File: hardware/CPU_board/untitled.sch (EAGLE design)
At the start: 60 parts, among them IC1 MAX232ECWE, IC2 MAX232ECWE, IC3 AM29F040J, IC4 74HCT138D, IC5 LM2596S, J2 POWER_JACKSLT, U1 AS6C4008-55SIN, Y1 CRYSTAL-GROUNDEDSMD-5X3.2

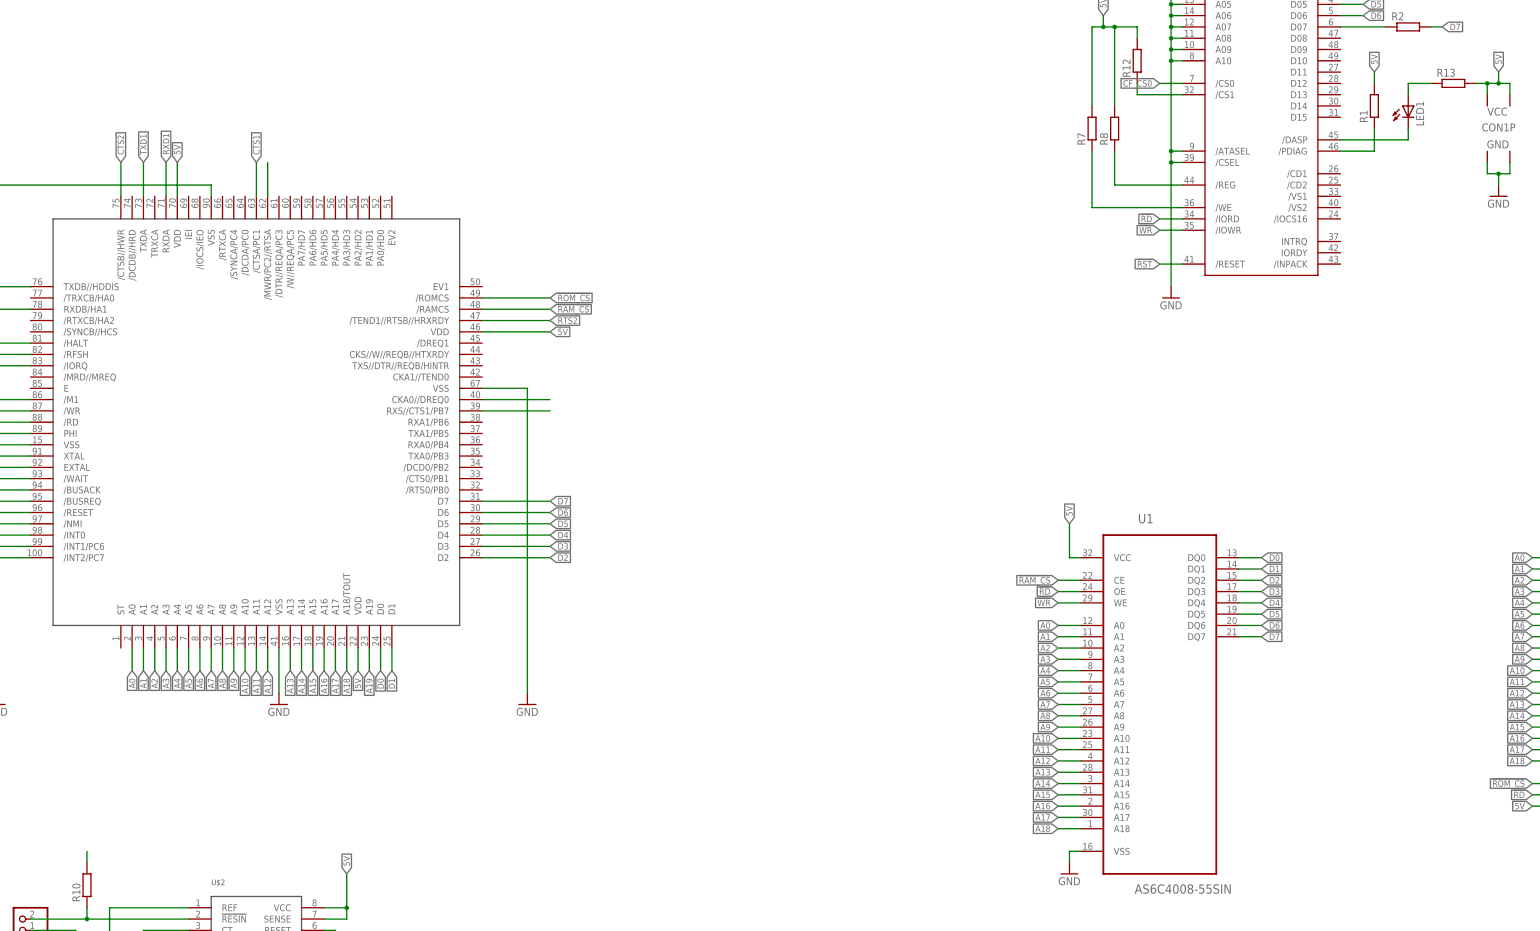
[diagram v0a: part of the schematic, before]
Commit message: Connector instead LED on board
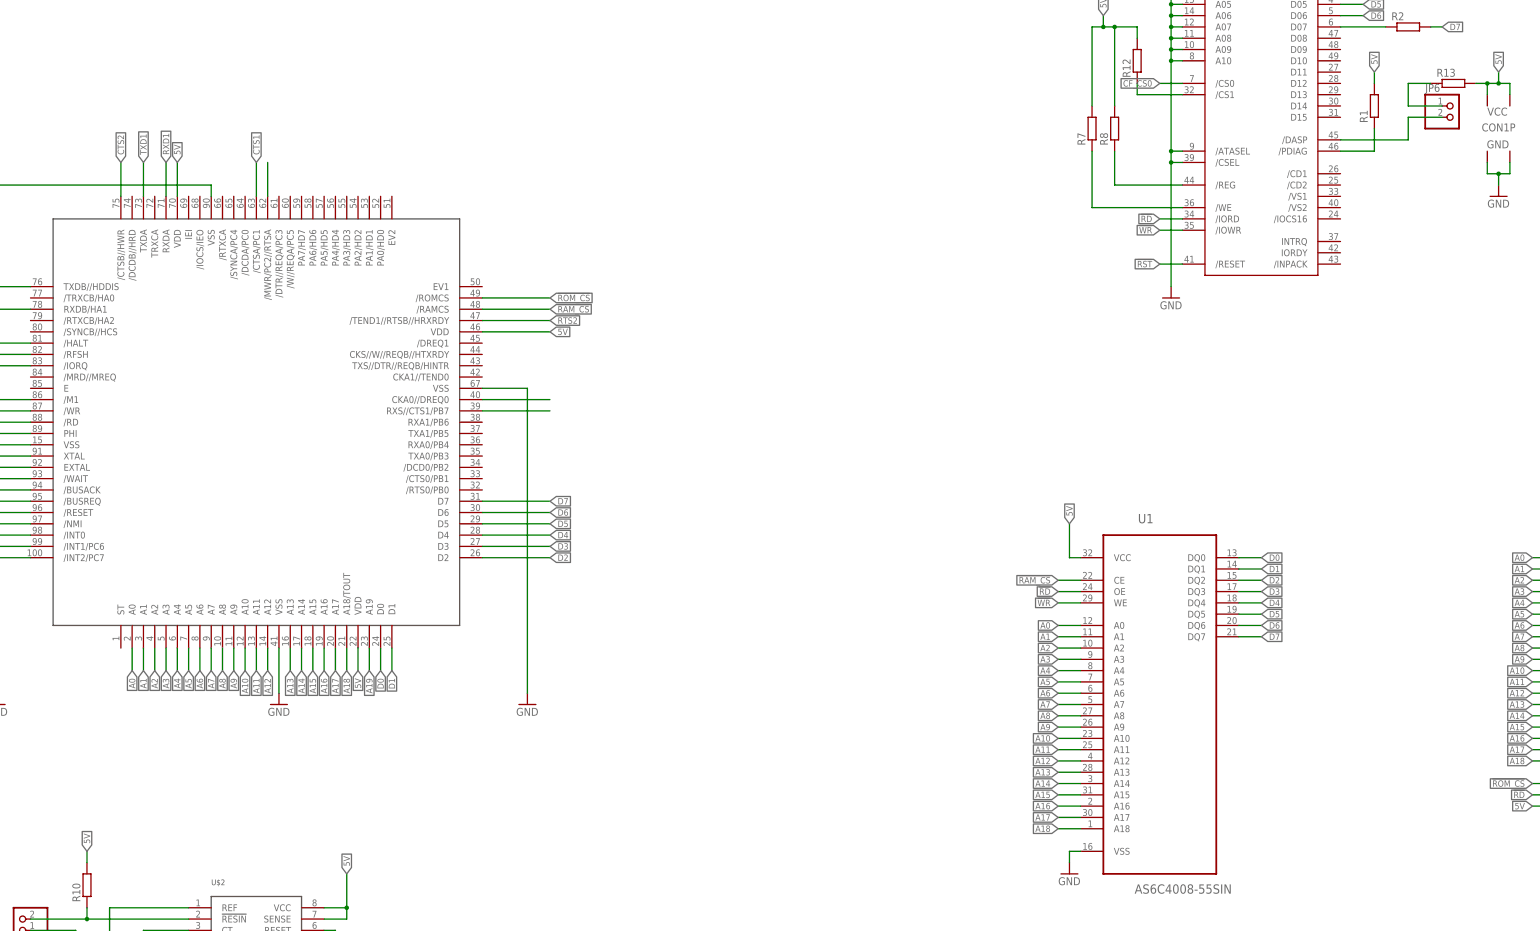
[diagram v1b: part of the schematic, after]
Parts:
- removed LED1: (no value), led:LED5MM
- added JP6: (no value), pinhead:PINHD-1X2
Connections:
- net N$32: now also JP6.1; no longer LED1.A
- net N$33: now also JP6.2; no longer LED1.C
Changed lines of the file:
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@@
 <part name="R12" library="rcl" deviceset="R-EU_" device="R0603"/>
 <part name="R13" library="rcl" deviceset="R-EU_" device="R0603"/>
-<part name="LED1" library="led" deviceset="LED" device="5MM"/>
 <part name="R2" library="rcl" deviceset="R-EU_" device="R0603"/>
 <part name="IC4" library="74xx-eu" deviceset="74*138" device="D" technology="HCT"/>
@@
 <part name="GND16" library="supply1" deviceset="GND" device=""/>
 <part name="R10" library="rcl" deviceset="R-EU_" device="R0603"/>
+<part name="JP6" library="pinhead" deviceset="PINHD-1X2" device=""/>
 </parts>
 <sheets>
@@
 <instance part="R12" gate="G$1" x="284.48" y="167.64" rot="R90"/>
 <instance part="R13" gate="G$1" x="355.6" y="162.56"/>
-<instance part="LED1" gate="G$1" x="345.44" y="157.48"/>
 <instance part="R2" gate="G$1" x="345.44" y="175.26"/>
 <instance part="IC4" gate="A" x="-203.2" y="15.24"/>
@@
 <instance part="GND16" gate="1" x="45.72" y="-45.72"/>
 <instance part="R10" gate="G$1" x="48.26" y="-17.78" rot="R90"/>
+<instance part="JP6" gate="G$1" x="355.6" y="154.94"/>
 </instances>
 <busses>
@@
 <pinref part="R10" gate="G$1" pin="2"/>
 <wire x1="48.26" y1="-12.7" x2="48.26" y2="-10.16" width="0.1524" layer="91"/>
+<label x="48.26" y="-10.16" size="1.4224" layer="95" rot="R90" xref="yes"/>
 </segment>
 </net>
@@
 <segment>
 <pinref part="R13" gate="G$1" pin="1"/>
-<pinref part="LED1" gate="G$1" pin="A"/>
 <wire x1="350.52" y1="162.56" x2="345.44" y2="162.56" width="0.1524" layer="91"/>
-<wire x1="345.44" y1="162.56" x2="345.44" y2="160.02" width="0.1524" layer="91"/>
+<pinref part="JP6" gate="G$1" pin="1"/>
+<wire x1="353.06" y1="157.48" x2="345.44" y2="157.48" width="0.1524" layer="91"/>
+<wire x1="345.44" y1="157.48" x2="345.44" y2="162.56" width="0.1524" layer="91"/>
 </segment>
 </net>
@@
 <segment>
 <pinref part="CON1" gate="G$1" pin="/DASP"/>
-<pinref part="LED1" gate="G$1" pin="C"/>
 <wire x1="330.2" y1="149.86" x2="345.44" y2="149.86" width="0.1524" layer="91"/>
-<wire x1="345.44" y1="149.86" x2="345.44" y2="152.4" width="0.1524" layer="91"/>
-</segment>
-</net>
+<pinref part="JP6" gate="G$1" pin="2"/>
+<wire x1="353.06" y1="154.94" x2="345.44" y2="154.94" width="0.1524" layer="91"/>
+<wire x1="345.44" y1="154.94" x2="345.44" y2="149.86" width="0.1524" layer="91"/>
+</segment>
+</net>

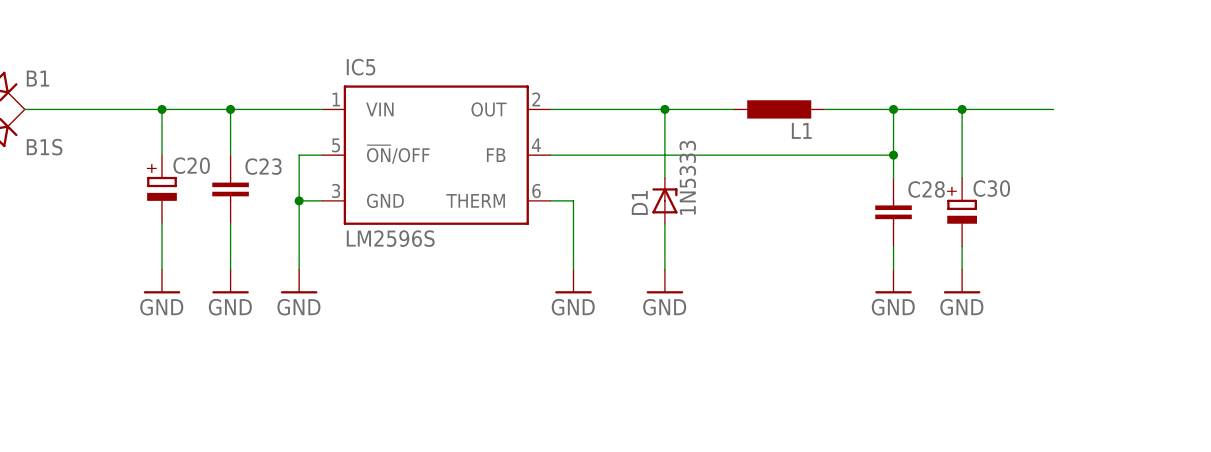
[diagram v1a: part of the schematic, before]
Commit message: Power circuit updated
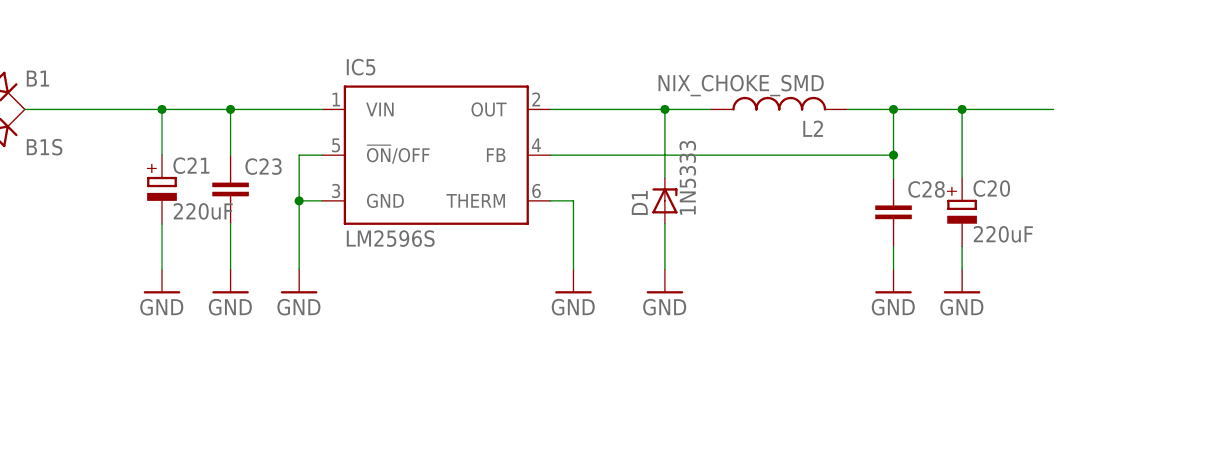
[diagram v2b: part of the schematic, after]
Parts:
- removed C30: (no value), rcl:CPOL-EUE3.5-8
- removed L1: (no value), rcl:L-EU6000-XXX-RC
- added C21: 220uF, rcl:CPOL-EU153CLV-0810
- added L2: NIX_CHOKE_SMD, mw:NIX_CHOKE_SMD
- C20: value (none) -> 220uF; device rcl:CPOL-EUE3.5-8 -> rcl:CPOL-EU153CLV-0810
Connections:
- net 5V: now also C20.+, L2.2; no longer C30.+, L1.2
- net GND: now also C21.-; no longer C30.-
- net N$22: now also C21.+; no longer C20.+
- net N$23: now also L2.1; no longer L1.1
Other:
- moved on the sheet: C20
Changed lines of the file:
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@@
 <part name="F1" library="polyfuse-smd_10" deviceset="?" device="1206L" technology="012" value="1206L012"/>
 <part name="J2" library="SparkFun-Connectors" deviceset="POWER_JACK" device="SLT"/>
-<part name="C20" library="rcl" deviceset="CPOL-EU" device="E3.5-8"/>
 <part name="GND52" library="supply1" deviceset="GND" device=""/>
 <part name="GND58" library="supply1" deviceset="GND" device=""/>
@@
 <part name="GND34" library="supply1" deviceset="GND" device=""/>
 <part name="GND56" library="supply1" deviceset="GND" device=""/>
-<part name="L1" library="rcl" deviceset="L-EU" device="6000-XXX-RC"/>
-<part name="C30" library="rcl" deviceset="CPOL-EU" device="E3.5-8"/>
 <part name="GND57" library="supply1" deviceset="GND" device=""/>
 <part name="U1" library="Alliance_Memory_By_element14_Batch_1" deviceset="AS6C4008-55SIN" device=""/>
@@
 <part name="R10" library="rcl" deviceset="R-EU_" device="R0603"/>
 <part name="JP6" library="pinhead" deviceset="PINHD-1X2" device=""/>
+<part name="C21" library="rcl" deviceset="CPOL-EU" device="153CLV-0810" value="220uF"/>
+<part name="C20" library="rcl" deviceset="CPOL-EU" device="153CLV-0810" value="220uF"/>
+<part name="L2" library="mw" deviceset="NIX_CHOKE_SMD" device=""/>
 </parts>
 <sheets>
@@
 <instance part="F1" gate="G$1" x="-236.22" y="274.32" rot="R180"/>
 <instance part="J2" gate="G$1" x="-248.92" y="266.7"/>
-<instance part="C20" gate="G$1" x="-195.58" y="266.7"/>
 <instance part="GND52" gate="1" x="-195.58" y="254"/>
 <instance part="GND58" gate="1" x="-180.34" y="254"/>
@@
 <instance part="GND34" gate="1" x="-114.3" y="254"/>
 <instance part="GND56" gate="1" x="-187.96" y="254"/>
-<instance part="L1" gate="G$1" x="-127" y="274.32" rot="R90"/>
-<instance part="C30" gate="G$1" x="-106.68" y="264.16"/>
 <instance part="GND57" gate="1" x="-106.68" y="254"/>
 <instance part="U1" gate="A" x="289.56" y="25.4"/>
@@
 <instance part="R10" gate="G$1" x="48.26" y="-17.78" rot="R90"/>
 <instance part="JP6" gate="G$1" x="355.6" y="154.94"/>
+<instance part="C21" gate="G$1" x="-195.58" y="266.7"/>
+<instance part="C20" gate="G$1" x="-106.68" y="264.16"/>
+<instance part="L2" gate="G$1" x="-127" y="274.32" rot="R90"/>
 </instances>
 <busses>
@@
 </segment>
 <segment>
-<pinref part="C20" gate="G$1" pin="-"/>
 <pinref part="GND52" gate="1" pin="GND"/>
-<wire x1="-195.58" y1="256.54" x2="-195.58" y2="261.62" width="0.1524" layer="91"/>
+<pinref part="C21" gate="G$1" pin="-"/>
+<wire x1="-195.58" y1="261.62" x2="-195.58" y2="256.54" width="0.1524" layer="91"/>
 </segment>
 <segment>
@@
 </segment>
 <segment>
-<pinref part="C30" gate="G$1" pin="-"/>
 <pinref part="GND57" gate="1" pin="GND"/>
-<wire x1="-106.68" y1="256.54" x2="-106.68" y2="259.08" width="0.1524" layer="91"/>
+<pinref part="C20" gate="G$1" pin="-"/>
+<wire x1="-106.68" y1="259.08" x2="-106.68" y2="256.54" width="0.1524" layer="91"/>
 </segment>
 <segment>
@@
 <wire x1="-114.3" y1="266.7" x2="-114.3" y2="269.24" width="0.1524" layer="91"/>
 <junction x="-114.3" y="269.24"/>
-<pinref part="L1" gate="G$1" pin="2"/>
-<wire x1="-121.92" y1="274.32" x2="-114.3" y2="274.32" width="0.1524" layer="91"/>
-<pinref part="C30" gate="G$1" pin="+"/>
-<wire x1="-106.68" y1="266.7" x2="-106.68" y2="274.32" width="0.1524" layer="91"/>
 <junction x="-106.68" y="274.32"/>
+<pinref part="C20" gate="G$1" pin="+"/>
+<wire x1="-106.68" y1="274.32" x2="-106.68" y2="266.7" width="0.1524" layer="91"/>
+<pinref part="L2" gate="G$1" pin="2"/>
+<wire x1="-119.38" y1="274.32" x2="-114.3" y2="274.32" width="0.1524" layer="91"/>
 </segment>
 <segment>
@@
 <net name="N$22" class="0">
 <segment>
-<pinref part="C20" gate="G$1" pin="+"/>
 <wire x1="-195.58" y1="274.32" x2="-187.96" y2="274.32" width="0.1524" layer="91"/>
 <wire x1="-187.96" y1="274.32" x2="-177.8" y2="274.32" width="0.1524" layer="91"/>
-<wire x1="-195.58" y1="269.24" x2="-195.58" y2="274.32" width="0.1524" layer="91"/>
 <pinref part="IC5" gate="G$1" pin="VIN"/>
 <pinref part="B1" gate="G$1" pin="+"/>
@@
 <wire x1="-187.96" y1="269.24" x2="-187.96" y2="274.32" width="0.1524" layer="91"/>
 <junction x="-187.96" y="274.32"/>
+<pinref part="C21" gate="G$1" pin="+"/>
+<wire x1="-195.58" y1="269.24" x2="-195.58" y2="274.32" width="0.1524" layer="91"/>
 </segment>
 </net>
@@
 <junction x="-139.7" y="274.32"/>
 <pinref part="IC5" gate="G$1" pin="OUT"/>
-<pinref part="L1" gate="G$1" pin="1"/>
-<wire x1="-132.08" y1="274.32" x2="-139.7" y2="274.32" width="0.1524" layer="91"/>
-</segment>
-</net>
+<pinref part="L2" gate="G$1" pin="1"/>
+<wire x1="-134.62" y1="274.32" x2="-139.7" y2="274.32" width="0.1524" layer="91"/>
+</segment>
+</net>
